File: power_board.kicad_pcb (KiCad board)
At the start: 2 copper layers, 156 x 110 mm, 110 parts, among them J1 Conn_01x01, J10 Conn_01x02, J11 Conn_01x02, J12 Conn_01x02, J13 Conn_01x02, J14 Conn_01x02, J15 Conn_01x02, J16 Conn_01x02, J17 Conn_01x02, J18 Conn_01x02, J19 Conn_01x02, J2 Conn_01x01, J20 Conn_01x03, J21 Conn_01x03, J22 Conn_01x03, J23 Conn_01x03, J24 Conn_01x03, J25 Conn_01x02, J26 Conn_01x02, J27 Conn_01x02, J28 Conn_01x02, J29 Conn_01x02, J3 Conn_01x01, J30 Conn_01x02, J4 ATX-24, J5 Conn_01x02, J6 Conn_01x02, J7 Conn_01x02, J8 Conn_01x02, J9 Conn_01x02, K1 SANYOU_SRD_Form_C, K2 SANYOU_SRD_Form_C, K3 SANYOU_SRD_Form_C, K4 SANYOU_SRD_Form_C, K5 SANYOU_SRD_Form_C, Q1 MMBT4401-7-F, Q10 MMBT4401-7-F, Q11 SI7113ADN-T1-GE3, Q12 Q_NMOS_GDS, Q13 Q_NMOS_GDS, Q14 Q_NMOS_GDS, Q15 Q_NMOS_GDS, Q16 Q_NMOS_GDS, Q2 MMBT4401-7-F, Q3 MMBT4401-7-F, Q4 SI7113ADN-T1-GE3, Q5 SI7113ADN-T1-GE3, Q6 MMBT4401-7-F, Q7 MMBT4401-7-F, Q8 SI7113ADN-T1-GE3, Q9 SI7113ADN-T1-GE3, U1 PCA9685PW, U2 PCA9685PW, U3 L298HN, U4 l6210, U5 L298HN, U6 l6210, U7 L298HN, U8 l6210

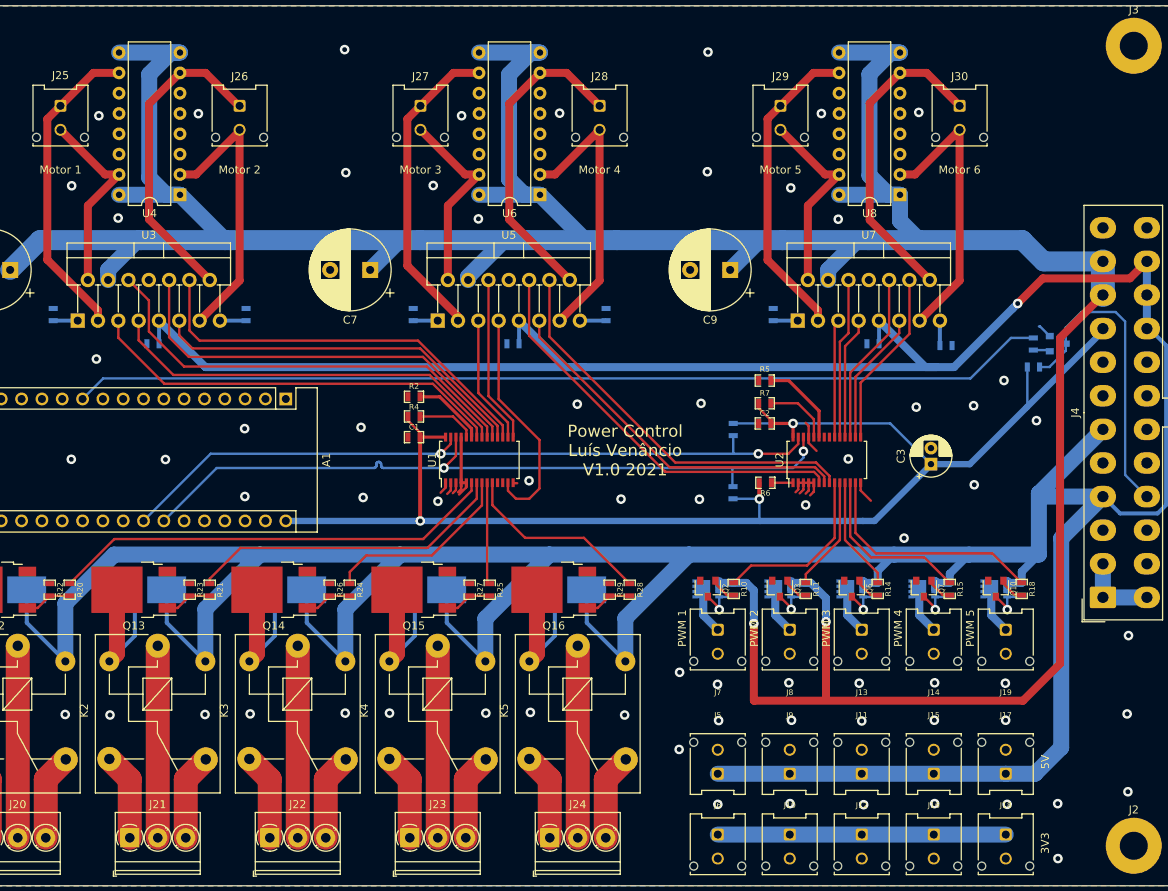
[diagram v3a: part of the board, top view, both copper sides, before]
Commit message: Changed sense resistor footprint
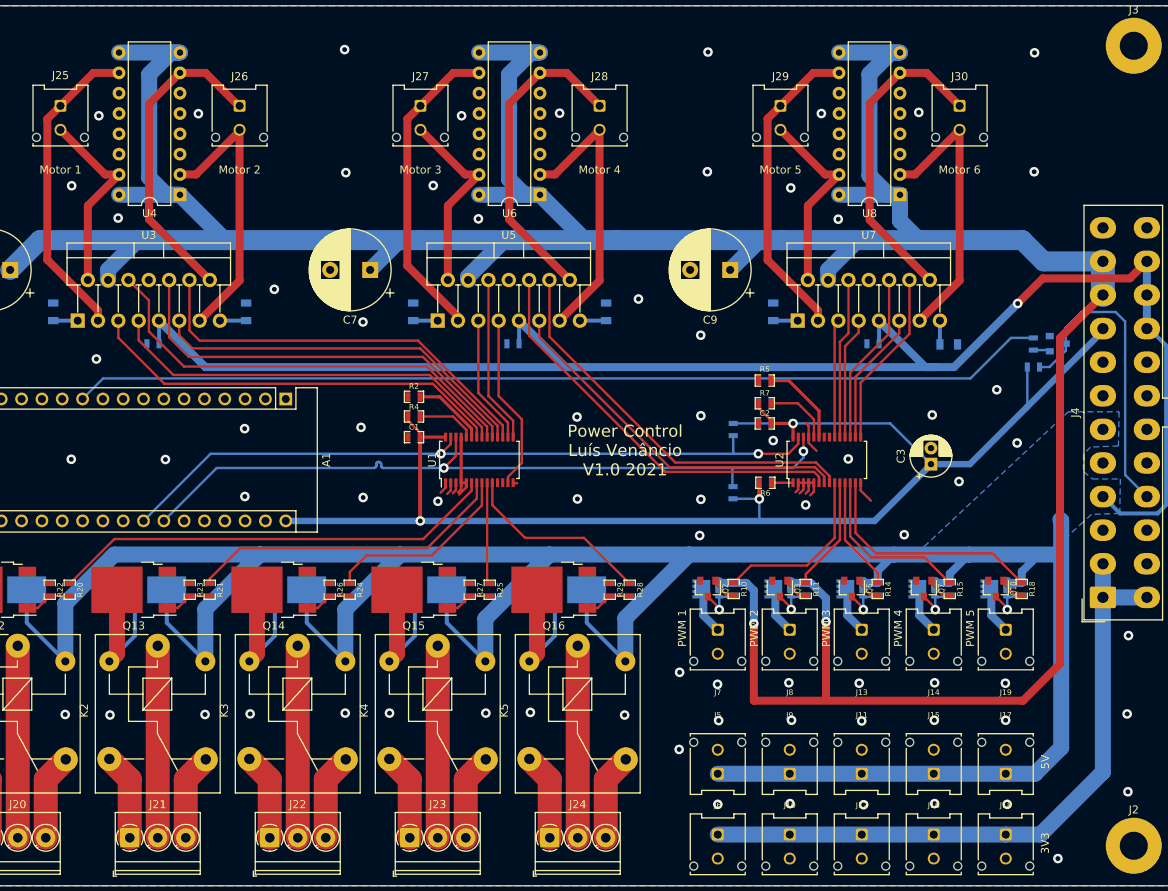
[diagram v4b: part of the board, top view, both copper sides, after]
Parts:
- R30, R31, R32, R33, R34, R35: footprint lsts_passives:R_0603 -> lsts_passives:R_0805
- moved R35 0.37 mm to (192.9, 82.3)
- moved R30 0.34 mm to (80.9, 78.3)
- moved R31 0.34 mm to (105.0, 78.3)
- moved R32 0.34 mm to (125.9, 78.3)
- moved R33 0.34 mm to (150.0, 78.3)
- moved R34 0.34 mm to (170.9, 78.3)
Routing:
- net +3V3: track 45.7 -> 82.9 mm
- net +5V: track 580.1 -> 550.7 mm
- net /MTR3_IN2: track 29.0 -> 22.2 mm
- net GND: track 31.5 -> 29.6 mm, vias 72 -> 77
- added copper zone on B.Cu, net +5V
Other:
- rule pad_to_mask_clearance: 0.051 -> 0

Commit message: Small fix
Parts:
- removed R9: 10kR, lsts_passives:R_0603
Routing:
- net /+5V_SB: track 177.0 -> 171.9 mm
- net Net-(J4-Pad16): track 38.8 -> 33.8 mm

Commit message: Ported to Kicad V7
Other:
- net class Default removed
- net class xclearance removed
